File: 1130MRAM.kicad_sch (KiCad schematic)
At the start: 159 parts, among them IC1 BSV52LT1G, IC10 BSV52LT1G, IC11 BSV52LT1G, IC12 BSV52LT1G, IC13 BSV52LT1G, IC14 BSV52LT1G, IC15 BSV52LT1G, IC16 BSV52LT1G, IC17 BSV52LT1G, IC18 BSV52LT1G, IC2 BSV52LT1G, IC3 BSV52LT1G, IC4 BSV52LT1G, IC5 BSV52LT1G, IC6 BSV52LT1G, IC7 BSV52LT1G, IC8 BSV52LT1G, IC9 BSV52LT1G, J1 Screw_Terminal_01x03, J1A09 SLTpad, J1A11 SLTpad, J2 Screw_Terminal_01x03, K1E09 SLTpad, K1E11 SLTpad, M1A09 SLTpad, M1A11 SLTpad, M1C09 SLTpad, M1D09 SLTpad, M1E09 SLTpad, M1E11 SLTpad, SW1 SLTpad, U1 MR0A16AYS35, U10 74LVC08A, U11 74LVC08A, U12 SN74LVC1G123DCUR, U13 SN74LVC1G123DCUR, U14 74HC00, U15 74HC86, U16 74HC86, U17 74HC86, U18 74HC86, U2 SN74LV240APWR, U3 SN74LV240APWR, U4 LDL1117, U5 SN74LVC1G123DCUR, U6 SN74LVC1G123DCUR, U7 74LVC08A, U8 74LVC08A, U9 74LVC08A

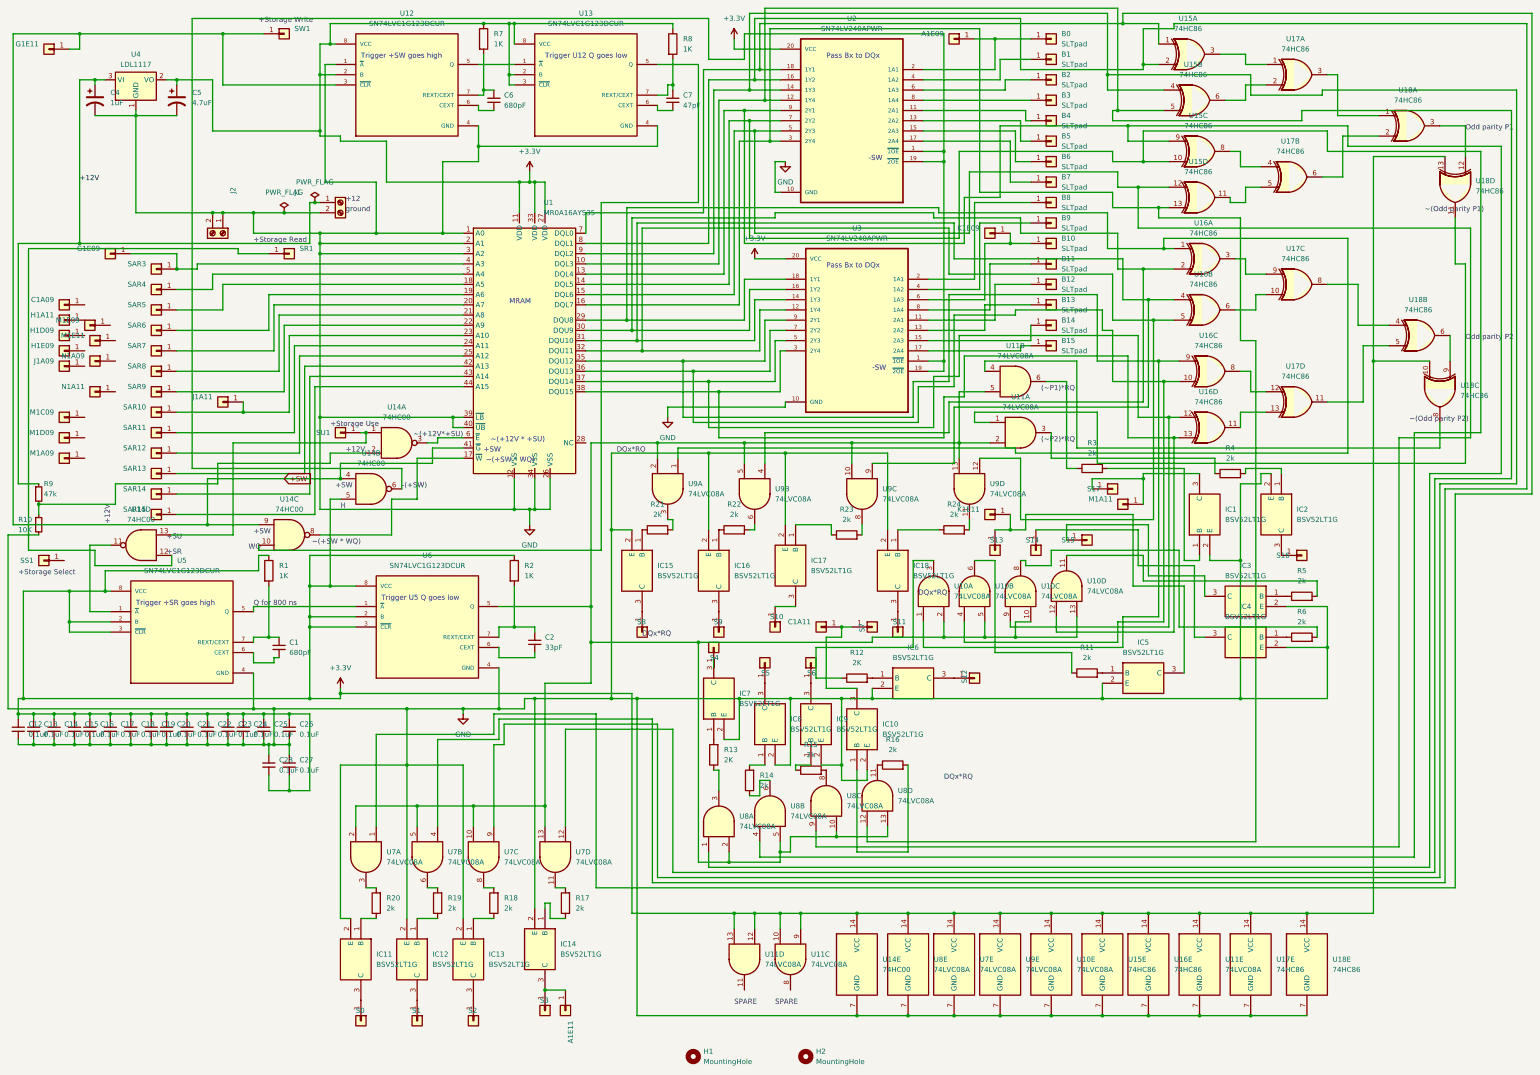
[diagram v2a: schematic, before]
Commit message: New version leveraging FPGA
Changed board to be driven by an FPGA
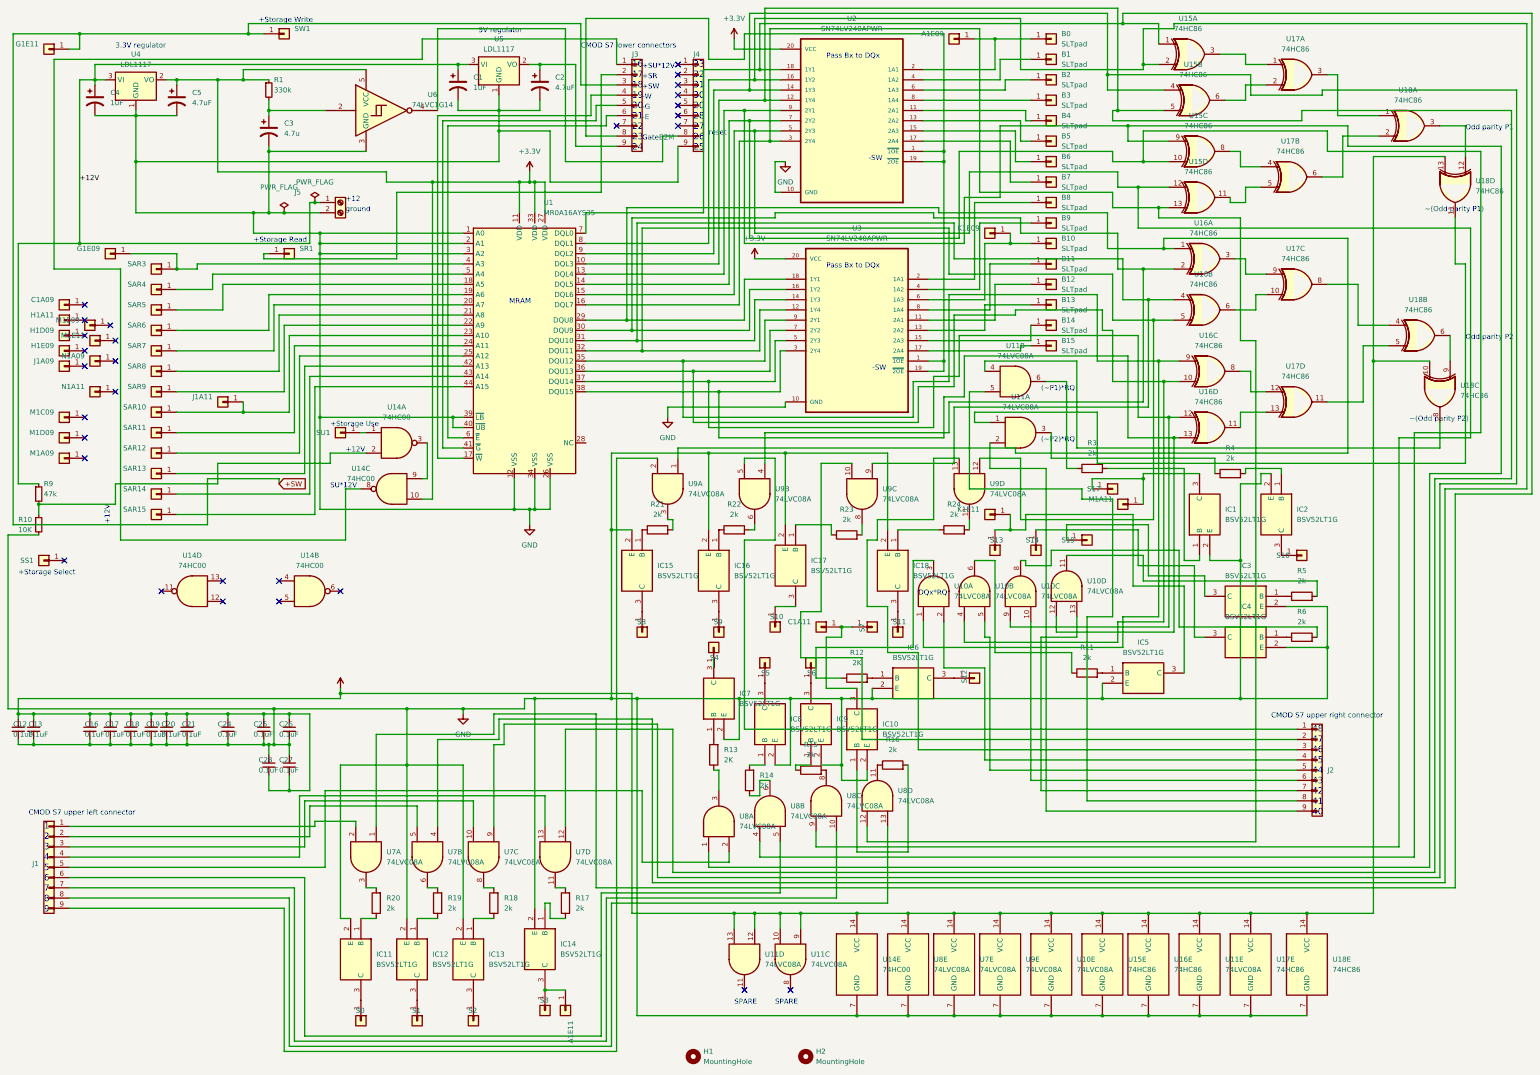
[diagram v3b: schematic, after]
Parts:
- removed C1, C6: 680pF, Capacitor_SMD:C_0805_2012Metric, symbol Device:C_Small
- removed C14, C15, C22, C23: 0.1uF, Capacitor_SMD:C_0603_1608Metric, symbol Device:C_Small
- removed C2: 33pF, Capacitor_SMD:C_0805_2012Metric, symbol Device:C_Small
- removed C7: 47pF, Capacitor_SMD:C_0805_2012Metric, symbol Device:C_Small
- removed J2: Screw_Terminal_01x03, Connector_Phoenix_MC_HighVoltage:PhoenixContact_MCV_1,5_2-G-5.08_1x02_P5.08mm_Vertical, symbol Connector:Screw_Terminal_01x02
- removed R1, R2, R7, R8: 1K, Resistor_SMD:R_0805_2012Metric, symbol Device:R
- removed U12, U13, U5, U6: SN74LVC1G123DCUR, 1130MRAM:sn74lvc1g123dcur, symbol 1130mram:SN74LVC1G123DCUR
- added C1: 1uF, Capacitor_SMD:C_0805_2012Metric, symbol Device:C_Polarized_US
- added C2: 4.7uF, Capacitor_SMD:C_0805_2012Metric, symbol Device:C_Polarized_US
- added C3: 4.7u, Capacitor_SMD:C_0805_2012Metric, symbol Device:C_Polarized_US
- added J1, J2, J3, J4: Conn_01x09_MountingPin, Connector_PinSocket_2.54mm:PinSocket_1x09_P2.54mm_Vertical, symbol Connector_Generic:Conn_01x09
- added R1: 330k, Resistor_SMD:R_0805_2012Metric, symbol Device:R_Small
- added U5: LDL1117, Package_TO_SOT_SMD:SOT-223-3_TabPin2, symbol Regulator_Linear:LD1117S18TR_SOT223
- added U6: 74LVC1G14, Package_TO_SOT_SMD:SOT-23-5_HandSoldering, symbol 74xGxx:74LVC1G14
- IC1, IC10, IC11, IC12, IC13, IC14, IC15, IC16, IC17, IC18, IC2, IC3, IC4, IC5, IC6, IC7, IC8, IC9: footprint SamacSys_Parts:SOT95P237X111-3N -> Package_TO_SOT_SMD:SOT-23
- renumbered J1 to J5
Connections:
- net +12V: now also C1.1, U5.3 (VI)
- net +3.3V: now also U14.10, R1.1, U6.5 (VCC); no longer U14.5
- net +SW: now also J3.3 (Pin_3); no longer U1.41 (~{G}), U14.4, U14.9
- net GND: now also C1.2, C2.2, C3.2, J4.9 (Pin_9), U5.1 (GND), U6.3 (GND)
- net at SU1.1 (Pin_1), U14.1: no longer U14.13
- net at U14.3: now also U14.9; no longer U1.6 (~{E})
- net at U2.1 (~{1OE}), U2.19 (~{2OE}), U3.1 (~{1OE})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: now also J3.8 (Pin_8); no longer U14.6
- net at U14.8: now also J3.1 (Pin_1); no longer U1.17 (~{W})
- net at SR1.1 (Pin_1): now also J3.2 (Pin_2); no longer U14.12
- new net: C2.1, J3.9 (Pin_9), U5.2 (VO)
- new net: J2.5 (Pin_5), U10.5
- new net: J2.1 (Pin_1), U9.5
- new net: J2.7 (Pin_7), U10.13
- new net: J1.9 (Pin_9), U9.2
- new net: J1.3 (Pin_3), U7.10
- new net: J2.9 (Pin_9), U11.2
- new net: J3.4 (Pin_4), U1.17 (~{W})
- new net: J3.5 (Pin_5), U1.41 (~{G})
- new net: J3.6 (Pin_6), U1.6 (~{E})
- new net: C3.1, R1.2, U6.2
- new net: J1.5 (Pin_5), U8.2
- new net: J2.4 (Pin_4), U10.2
- new net: J1.1 (Pin_1), U7.2
- new net: J2.2 (Pin_2), U9.10
- new net: J2.3 (Pin_3), U9.13
- new net: J2.6 (Pin_6), U10.10
- new net: J2.8 (Pin_8), U11.5
- new net: J4.8 (Pin_8), U6.4
- new net: J1.4 (Pin_4), U7.13
- new net: J1.2 (Pin_2), U7.5
- new net: J1.6 (Pin_6), U8.5
- new net: J1.7 (Pin_7), U8.10
- new net: J1.8 (Pin_8), U8.13
- no-connect marks 0 -> 29
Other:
- note added: "+SU*12V"
- note added: "-E"
- note added: "-G"
- note added: "-W"
- note added: "1 2 3 4 5 6 7 8 9"
- note added: "16 17 18 19 20 21 22 23 24"
- note added: "3.3V regulator"
- note added: "33 32 31 30 20 28 27 26 25"
- note added: "48 47 46 45 44 43 42 41 40"
- note added: "5V regulator"
- note added: "CMOD S7 lower connectors"
- note added: "CMOD S7 upper left connector"
- note added: "CMOD S7 upper right connector"
- note added: "GateB2M"
- note added: "SU*12V"
- note added: "reset"
- note removed: "+SU"
- note removed: "-(+SW)"
- note removed: "H"
- note removed: "Q for 800 ns"
- note removed: "Trigger +SR goes high"
- note removed: "Trigger +SW goes high"
- note removed: "Trigger U12 Q goes low"
- note removed: "Trigger U5 Q goes low"
- note removed: "WQ"
- note removed: "~(+12V * +SU)"
- note removed: "~(+12V*+SU)"
- note removed: "~(+SW * WQ)"
- moved on the sheet: U14B, U14C, U14D
